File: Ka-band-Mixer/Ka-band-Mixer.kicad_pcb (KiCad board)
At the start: 4 copper layers, 55.9 x 41.9 mm, 75 parts, among them J1 Conn_01x02_Male, J2 Conn_01x02_Male, J3 Connector_Conn_01x02_Male, J4 Conn_01x05_Male, J5 SMA_END-frequencySintesizer, U1 ADF4150HV, U2 LT1962-3.3, U3 LT3010, U4 HMC739LP4E, U5 LT1962-5, U6 LT1962-5, U7 E_12_4, X1 IQXT-220-1

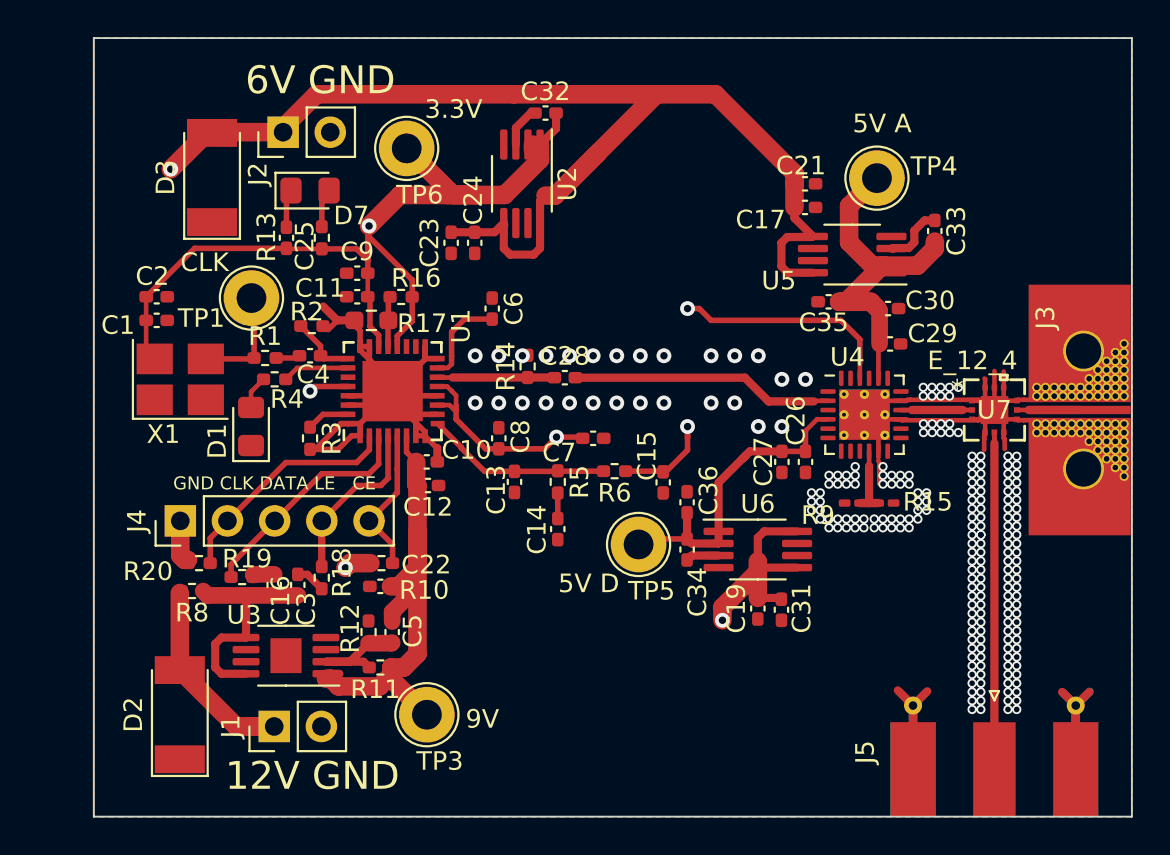
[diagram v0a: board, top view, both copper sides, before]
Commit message: ADD GND test probe
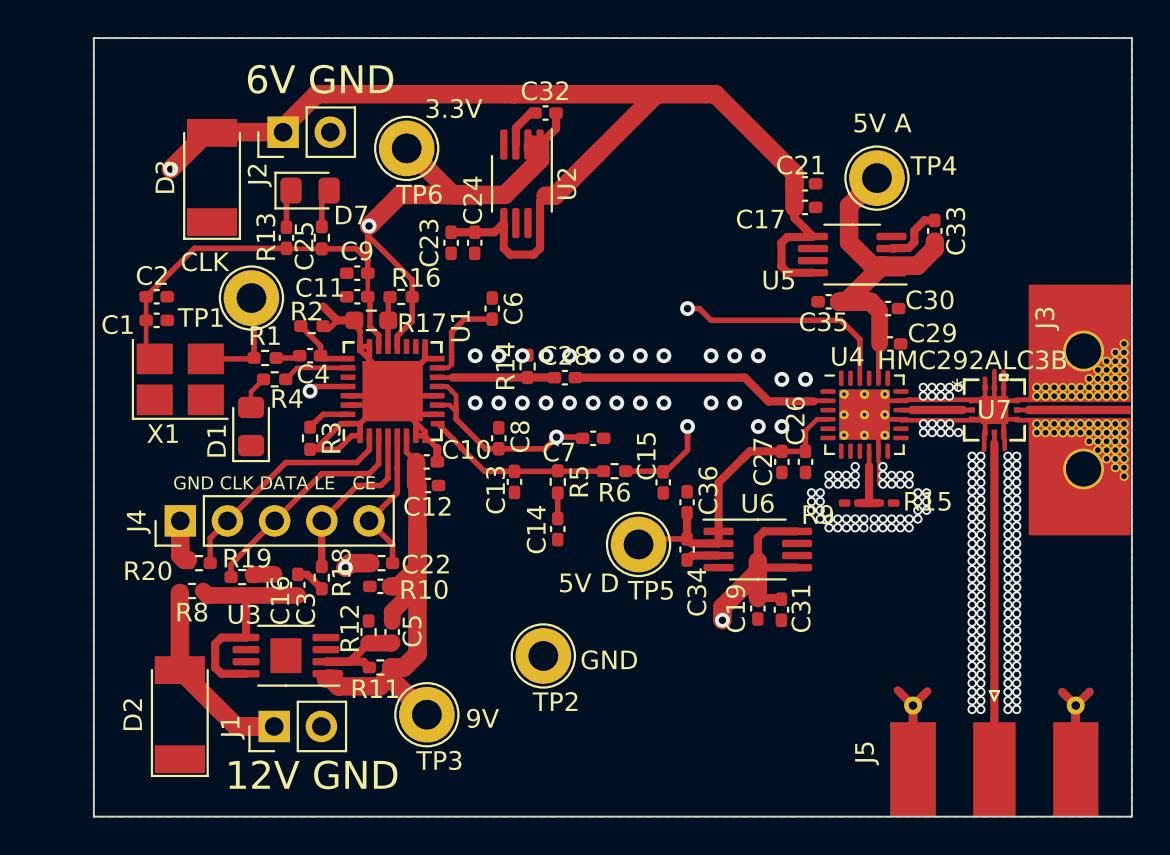
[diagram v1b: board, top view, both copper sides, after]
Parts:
- added TP2: TestPoint, TestPoint:TestPoint_Loop_D2.60mm_Drill1.6mm_Beaded, F.Cu at (116.5, 113.2)
- U7: value E_12_4 -> HMC292ALC3B
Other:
- board text added: "GND"

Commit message: Some fixes
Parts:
- added R7: 100r, Microwave_LO_Generator:R_0201_0603_HandSolder_mod, F.Cu at (112.3, 97.3)
- R14: value 51r -> 100r; footprint Resistor_SMD:R_0402_1005Metric_Pad0.72x0.64mm_HandSolder -> Microwave_LO_Generator:R_0201_0603_HandSolder_mod
- U7: value HMC292ALC3B -> E_12_4
- moved TP4 6.38 mm to (140.4, 89.8)
- moved C7 5.20 mm to (113.9, 101.6)
- moved R14 3.61 mm to (112.3, 99.1), turned to 270 degrees
- moved TP6 2.34 mm to (109.2, 88.2)
- moved C8 1.75 mm to (112.5, 100.6), turned to 180 degrees
- moved R15 1.72 mm to (134.9, 103.2)
- moved R9 1.72 mm to (133.1, 103.2)
- moved C30 1.55 mm to (135.1, 96.0)
- moved C26 1.41 mm to (130.6, 101.3)
- moved C29 0.64 mm to (135.1, 97.0)
- moved C27 0.36 mm to (129.5, 102.5)
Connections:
- U4 pad 1: (no net) -> 0
- U4 pad 12: (no net) -> 0
- U4 pad 13: (no net) -> 0
- U4 pad 14: (no net) -> 0
- U4 pad 18: (no net) -> 0
- U4 pad 19: (no net) -> 0
- U4 pad 21: (no net) -> 0
- U4 pad 23: (no net) -> 0
- U4 pad 24: (no net) -> 0
- U4 pad 3: (no net) -> 0
- U4 pad 5: (no net) -> 0
- U4 pad 6: (no net) -> 0
- U4 pad 7: (no net) -> 0
- U4 pad 8: (no net) -> 0
- U4 pad 9: (no net) -> 0
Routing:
- net 0: track 92.8 -> 307.9 mm, vias 218 -> 366
- net +3V3: track 109.1 -> 134.6 mm
- net +6V: track 133.7 -> 136.5 mm
- net +5VA: track 19.3 -> 17.4 mm
- net DIV16: track 6.55 -> 8.19 mm
- net Net-(R15-Pad1): track 3.77 -> 2.98 mm
- net +5VD: track 17.5 -> 16.9 mm

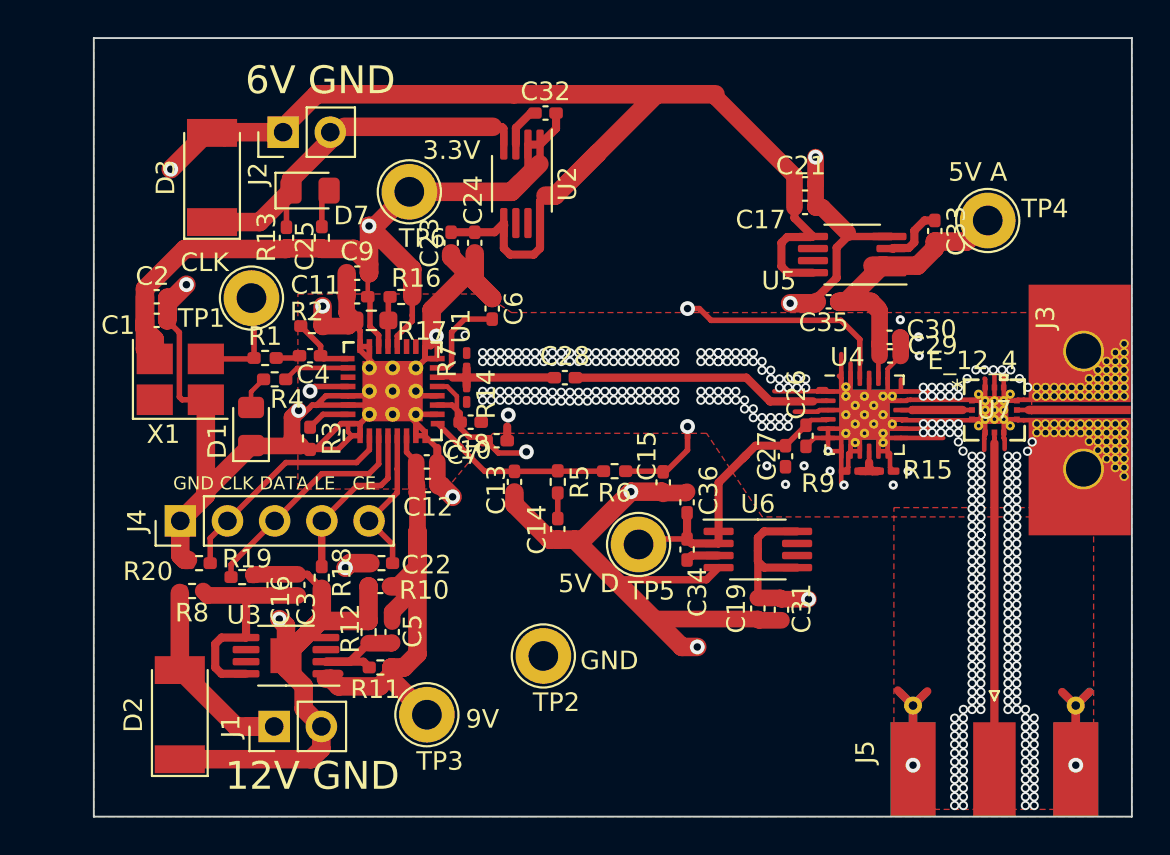
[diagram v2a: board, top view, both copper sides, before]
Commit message: Add stability hole
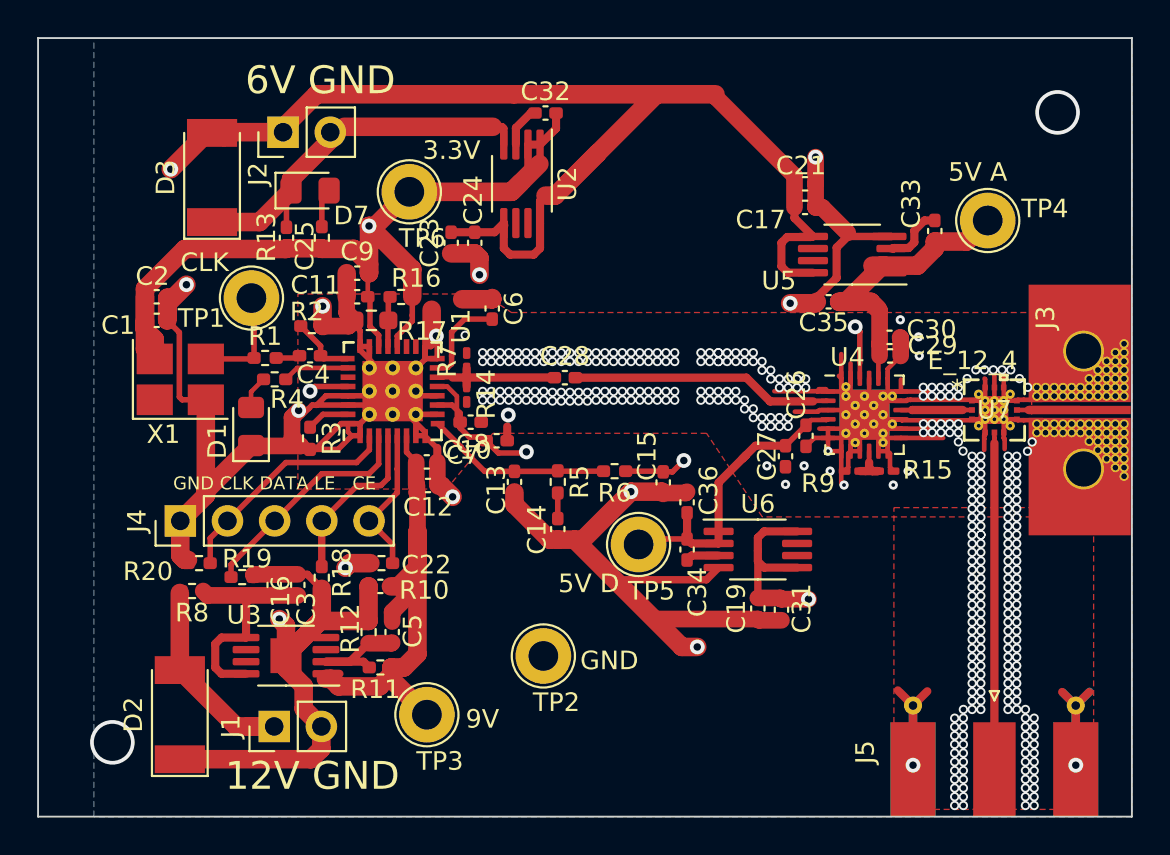
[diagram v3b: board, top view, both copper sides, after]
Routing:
- net 0: track 307.9 -> 303.1 mm, vias 366 -> 367
- net CPout: track 24.2 -> 22.0 mm
- net (no net): vias 0 -> 2
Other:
- board size 55.9 x 41.9 mm -> 58.9 x 41.9 mm

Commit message: Edit annular ring
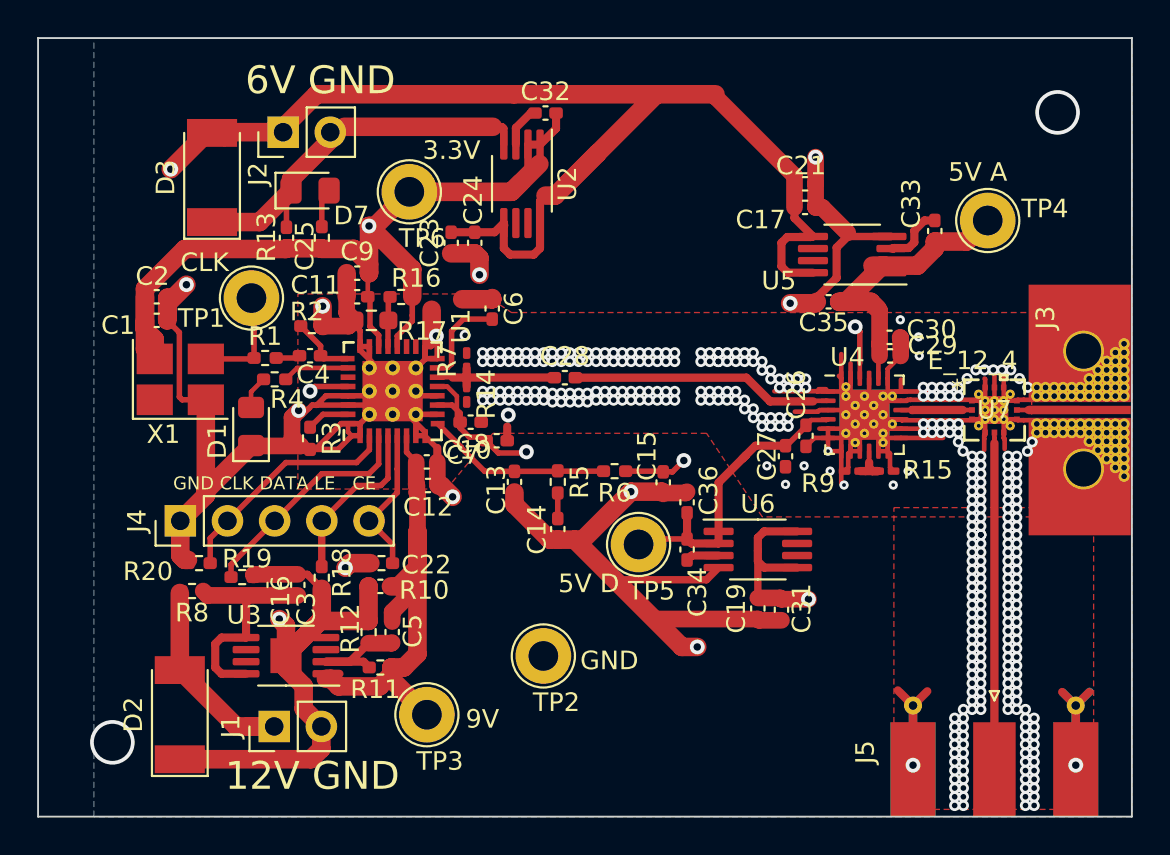
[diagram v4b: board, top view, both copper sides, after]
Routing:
- net +3V3: track 134.6 -> 128.3 mm
- net 0: vias 367 -> 368
- net (no net): vias 2 -> 1

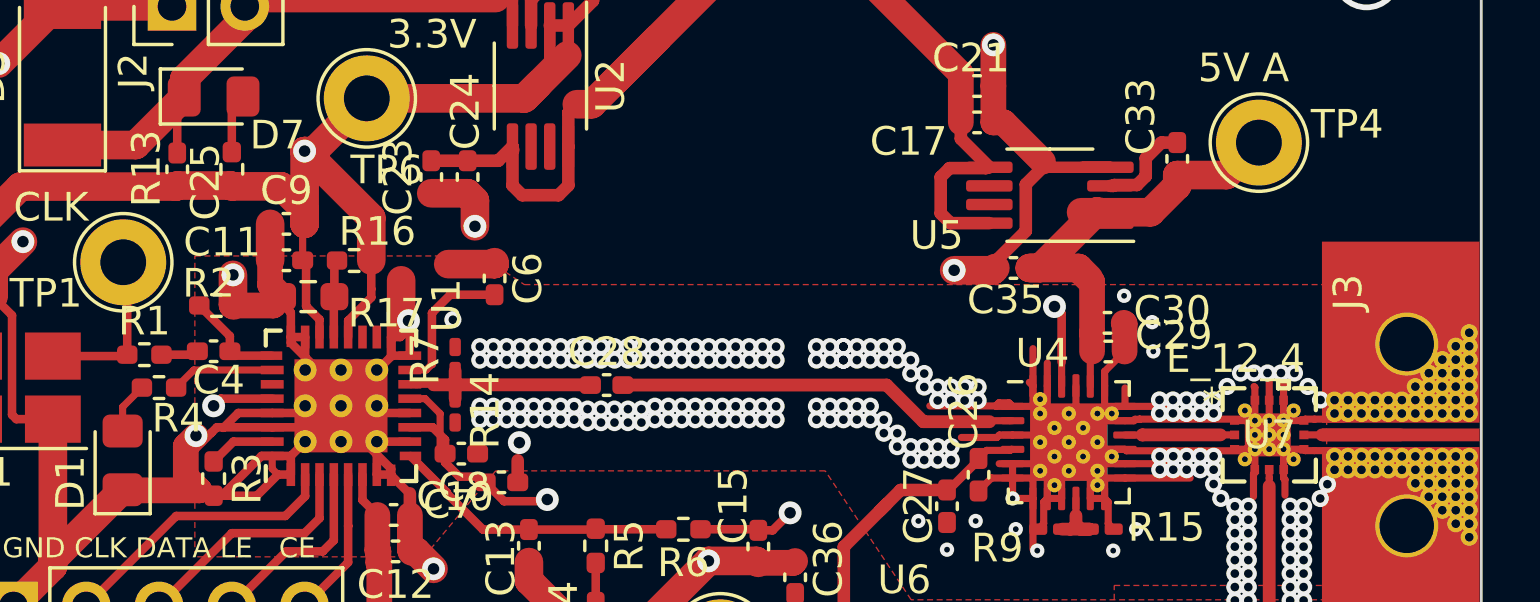
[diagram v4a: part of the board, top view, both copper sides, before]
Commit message: Remove PullDown PDBRF
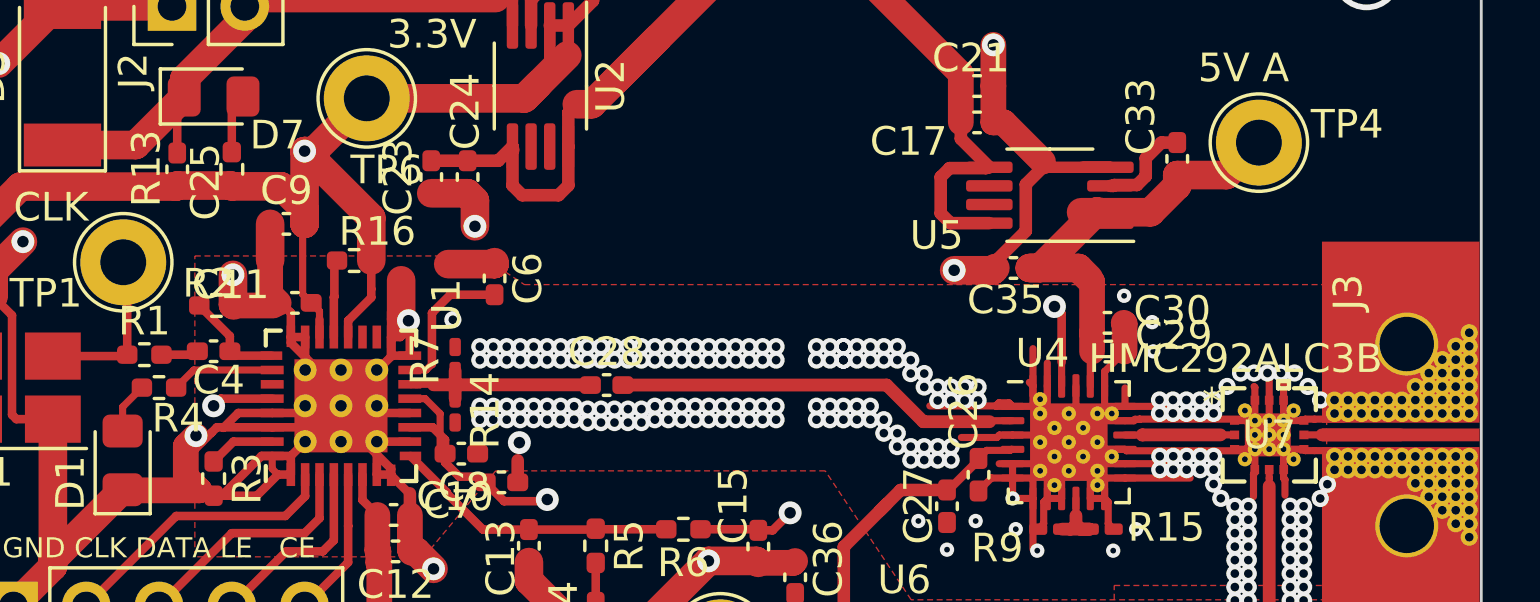
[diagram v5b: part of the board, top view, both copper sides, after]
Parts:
- removed R17: DNI, Resistor_SMD:R_0603_1608Metric_Pad0.98x0.95mm_HandSolder
- U7: value E_12_4 -> HMC292ALC3B
- moved C11 1.52 mm to (106.7, 95.4)
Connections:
- U1 pad 18: (no net) -> Net-(U1-Pad18)
- U1 pad 19: (no net) -> Net-(U1-Pad19)
- U1 pad 27: (no net) -> Net-(U1-Pad27)
- U2 pad 6: (no net) -> Net-(U2-Pad6)
- U2 pad 7: (no net) -> Net-(U2-Pad7)
- U3 pad 3: (no net) -> Net-(U3-Pad3)
- U3 pad 6: (no net) -> Net-(U3-Pad6)
- U3 pad 7: (no net) -> Net-(U3-Pad7)
- U5 pad 6: (no net) -> Net-(U5-Pad6)
- U5 pad 7: (no net) -> Net-(U5-Pad7)
- U6 pad 6: (no net) -> Net-(U6-Pad6)
- U6 pad 7: (no net) -> Net-(U6-Pad7)
- X1 pad 1: (no net) -> Net-(X1-Pad1)

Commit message: some_update
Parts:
- removed R16: 0, Resistor_SMD:R_0402_1005Metric_Pad0.72x0.64mm_HandSolder
- moved C9 1.75 mm to (106.7, 94.3)
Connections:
- U1 pad 21: Net-(R16-Pad2) -> +3V3
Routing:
- net Net-(R16-Pad2): track 2.74 -> 0.00 mm
- net 0: track 302.8 -> 300.4 mm
- net +3V3: track 128.3 -> 129.4 mm

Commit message: Update BOM
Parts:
- C28: footprint Capacitor_SMD:C_0402_1005Metric_Pad0.74x0.62mm_HandSolder -> Capacitor_SMD:C_0201_0603Metric_Pad0.64x0.40mm_HandSolder

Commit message: update bom
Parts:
- renumbered C12 to C10, C13 to C11, C14 to C12, C15 to C13, C16 to C14, C3 to C15, C5 to C16, C22 to C17, C23 to C18, C17 to C19, C19 to C20, C24 to C21, C21 to C22, C31 to C23, C32 to C24, C33 to C25, C34 to C26, C25 to C27, C35 to C28, C36 to C29, C4 to C3, C27 to C30, C26 to C31, C28 to C32, C29 to C33, C30 to C34, C6 to C4, C7 to C5, C8 to C6, C9 to C7, C10 to C8, C11 to C9, D7 to D4, J4 to J1, J1 to J2, J2 to J3, J3 to J4, R10 to R1, R6 to R10, R8 to R11, R11 to R12, R12 to R13, R13 to R14, R7 to R15, R9 to R16, R14 to R17, R15 to R18, R1 to R2, R18 to R3, R19 to R4, R20 to R5, R2 to R6, R3 to R7, R4 to R8, R5 to R9, U3 to U2, U2 to U3, U5 to U4, U6 to U5, U4 to U6
